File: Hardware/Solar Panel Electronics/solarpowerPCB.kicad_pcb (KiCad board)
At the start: 4 copper layers, 57.8 x 69.2 mm, 151 parts, among them J1 Screw_Terminal_SolarPanel_Inp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, J10 Screw_Terminal_SolarPanel_Inp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, J11 Screw_Terminal_SolarPanel_Inp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, J12 NTC Connector, J13 Battery Connector, J14 Screw_Terminal_5VRail, J2 Screw_Terminal_SolarPanel_Inp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, J3 Conn_01x02_Male, J4 Conn_01x06_Male, J5 Conn_01x02_Male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

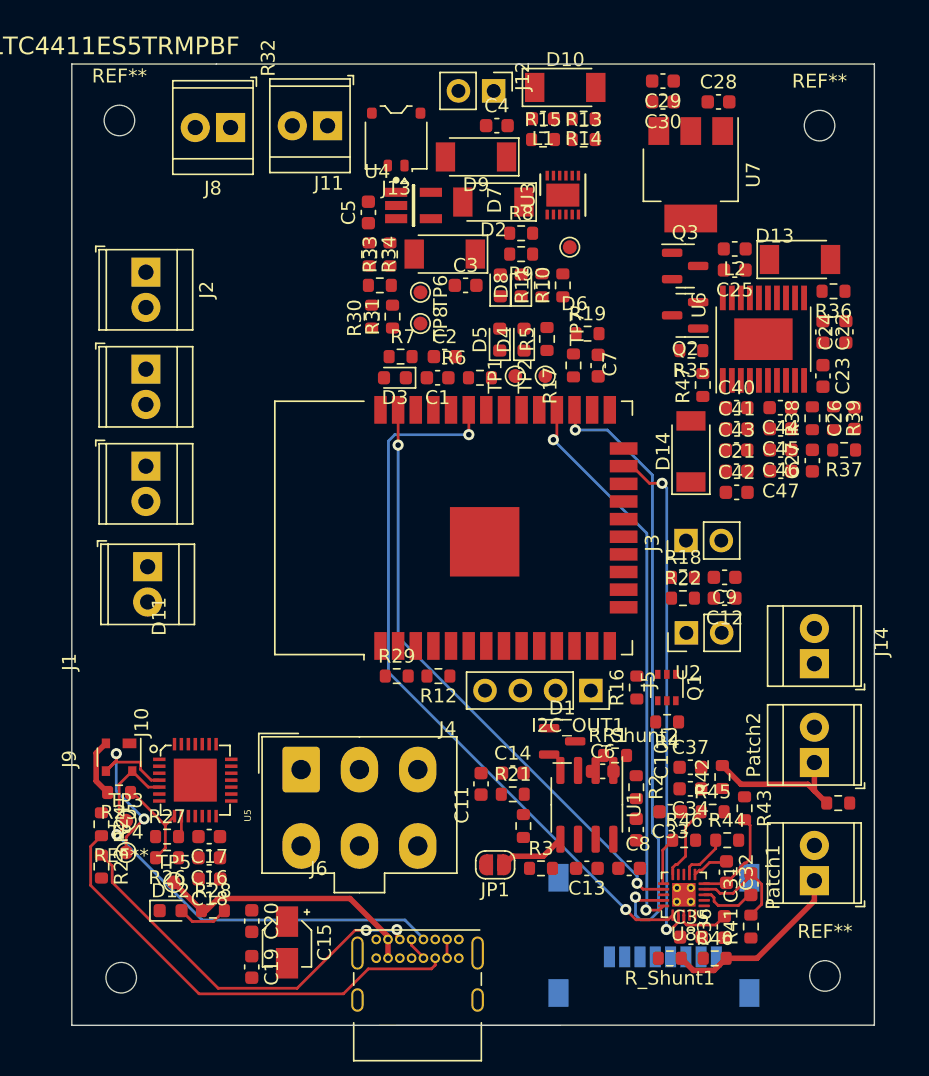
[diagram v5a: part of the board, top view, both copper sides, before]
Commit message: Added another ADS component. Layout and routing can be continued.
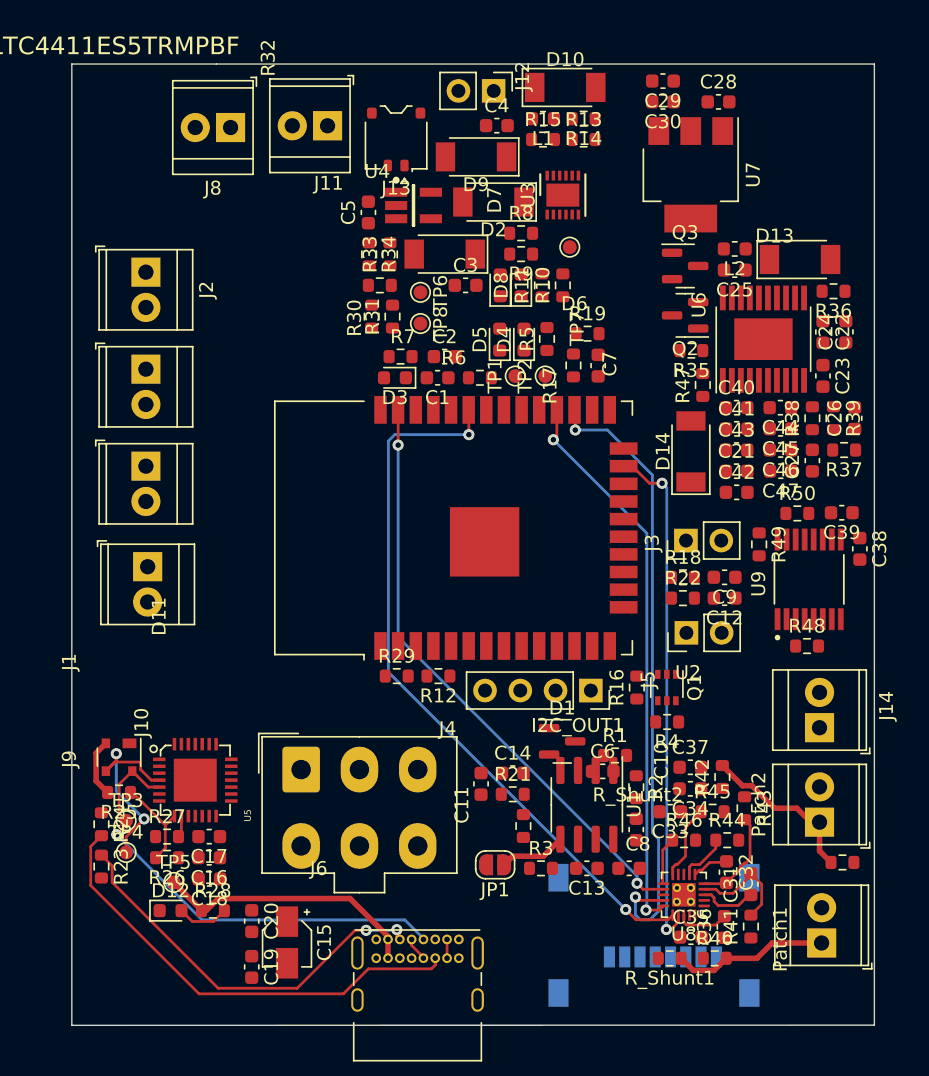
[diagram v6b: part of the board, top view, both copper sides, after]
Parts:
- removed REF** (x4): MountingHole_2.2mm_M2, MountingHole:MountingHole_2.2mm_M2
- added C38: 0.1uF, Capacitor_SMD:C_0603_1608Metric, F.Cu at (82.9, 102.5)
- added C39: 10uF, Capacitor_SMD:C_0603_1608Metric, F.Cu at (81.6, 99.9)
- added R48: 10k, Resistor_SMD:R_0603_1608Metric, F.Cu at (79.1, 109.5)
- added R49: 1k, Resistor_SMD:R_0603_1608Metric, F.Cu at (75.7, 102.2)
- added R50: 1k, Resistor_SMD:R_0603_1608Metric, F.Cu at (78.4, 99.9)
- added U9: ADS1219IPWT, ADS1219IPWT:SOP65P640X120-16N, F.Cu at (79.2, 104.7)
- moved J14 4.62 mm to (80.0, 115.3)
- moved Patch1 4.52 mm to (80.2, 130.8)
- moved Patch2 4.31 mm to (80.0, 122.2)
- moved R_Shunt2 4.28 mm to (81.7, 125.0)
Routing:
- net Net-(Patch1-Pad1): track 13.5 -> 11.3 mm
- net Net-(Patch2-Pad1): track 10.7 -> 11.9 mm

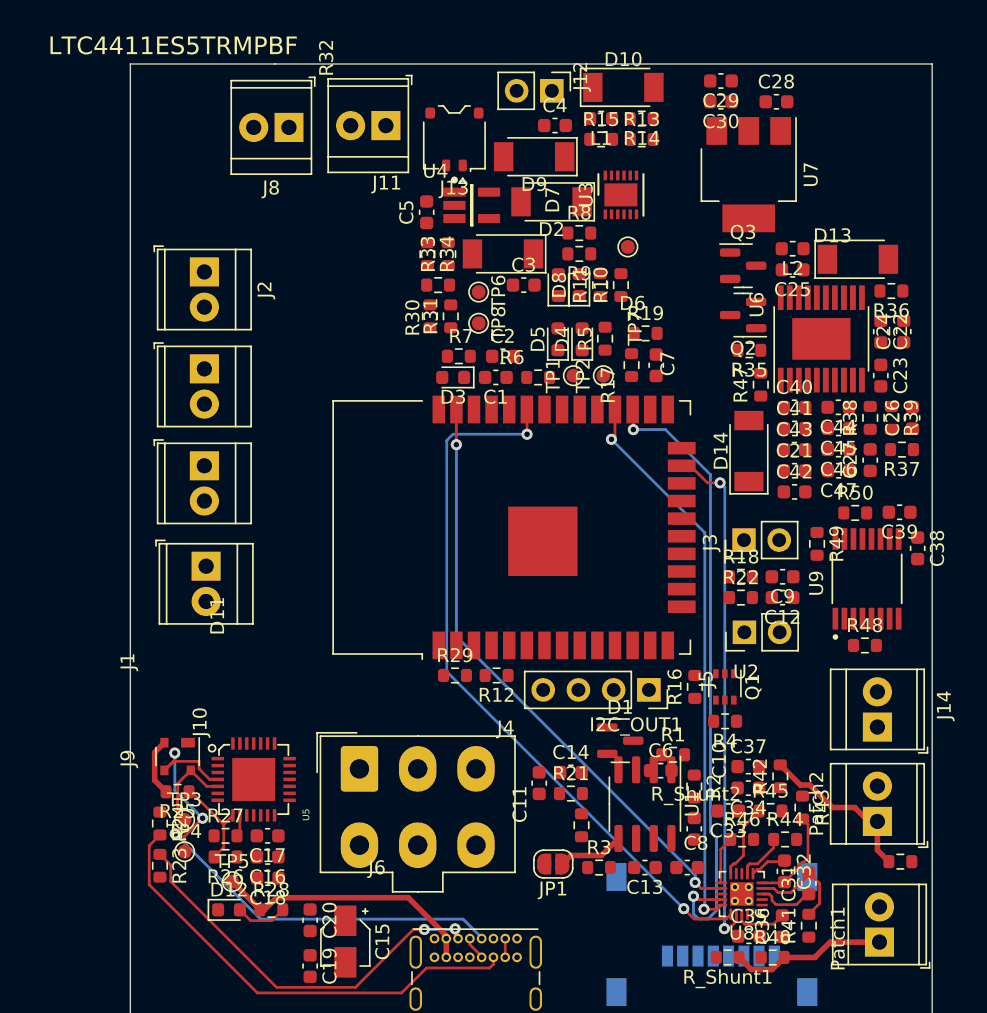
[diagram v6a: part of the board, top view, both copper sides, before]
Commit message: Top half routing done
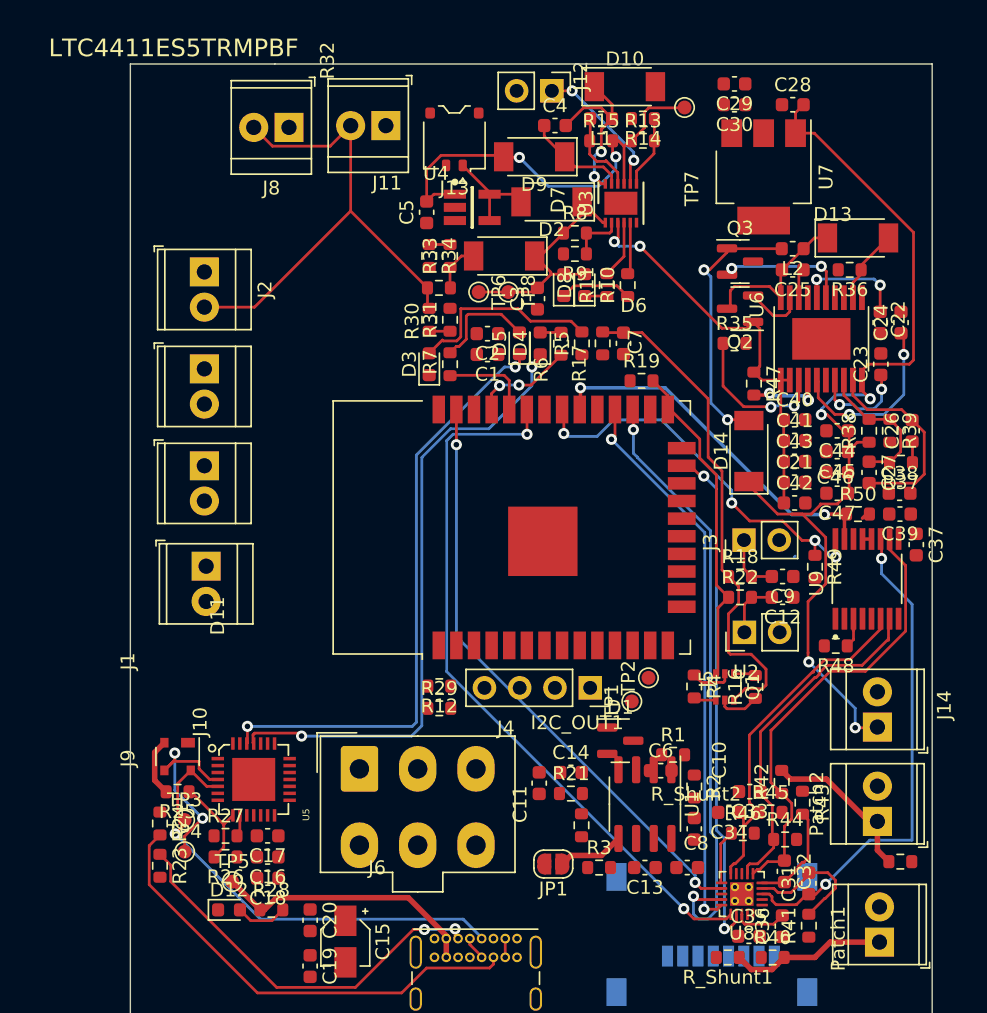
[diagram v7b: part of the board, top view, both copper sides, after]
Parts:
- moved TP1 23.8 mm to (62.3, 113.5)
- moved TP2 22.0 mm to (63.5, 111.8)
- moved C37 20.1 mm to (82.8, 102.2), turned to -90 degrees
- moved TP7 10.8 mm to (66.1, 70.7)
- moved R16 4.36 mm to (71.2, 112.5)
- moved I2C_OUT1 4.24 mm to (59.3, 112.5)
- moved R12 4.20 mm to (48.4, 112.4)
- moved C38 4.18 mm to (81.6, 98.5), turned to 0 degrees
- moved R19 3.43 mm to (63.0, 90.4)
- moved R36 3.37 mm to (78.0, 82.4)
- moved R4 3.35 mm to (66.8, 112.4), turned to -90 degrees
- moved TP8 3.10 mm to (53.4, 84.0)
- moved D4 3.04 mm to (55.7, 87.7)
- moved R6 2.94 mm to (57.2, 87.7), turned to 90 degrees
- moved C7 2.84 mm to (61.7, 87.7)
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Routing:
- net /VoltageReg/V_reg: track 0.00 -> 71.9 mm, vias 0 -> 4
- net /VSolCharger: track 0.00 -> 47.9 mm, vias 0 -> 2
- net /RXD: track 0.00 -> 45.2 mm, vias 0 -> 2
- net /TXD: track 0.00 -> 43.6 mm, vias 0 -> 2
- net /Solar Charger/V_solarpanel: track 0.00 -> 37.1 mm
- net /EN: track 0.00 -> 36.2 mm
- net Net-(C5-Pad2): track 0.00 -> 32.0 mm, vias 0 -> 2
- net /ADC/AIN0P: track 4.15 -> 35.9 mm, vias 0 -> 2
- net /ADC/AIN1P: track 2.66 -> 32.7 mm
- net /SCL: track 0.00 -> 29.0 mm, vias 0 -> 4
- net /SDA: track 0.00 -> 26.4 mm, vias 0 -> 2
- net /BOOT: track 0.00 -> 23.9 mm
- net /ADC/AIN2P: track 3.59 -> 25.4 mm
- net /ADC/AIN3P: track 5.43 -> 25.9 mm
- net Net-(D14-Pad2): track 0.00 -> 19.5 mm, vias 0 -> 2
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
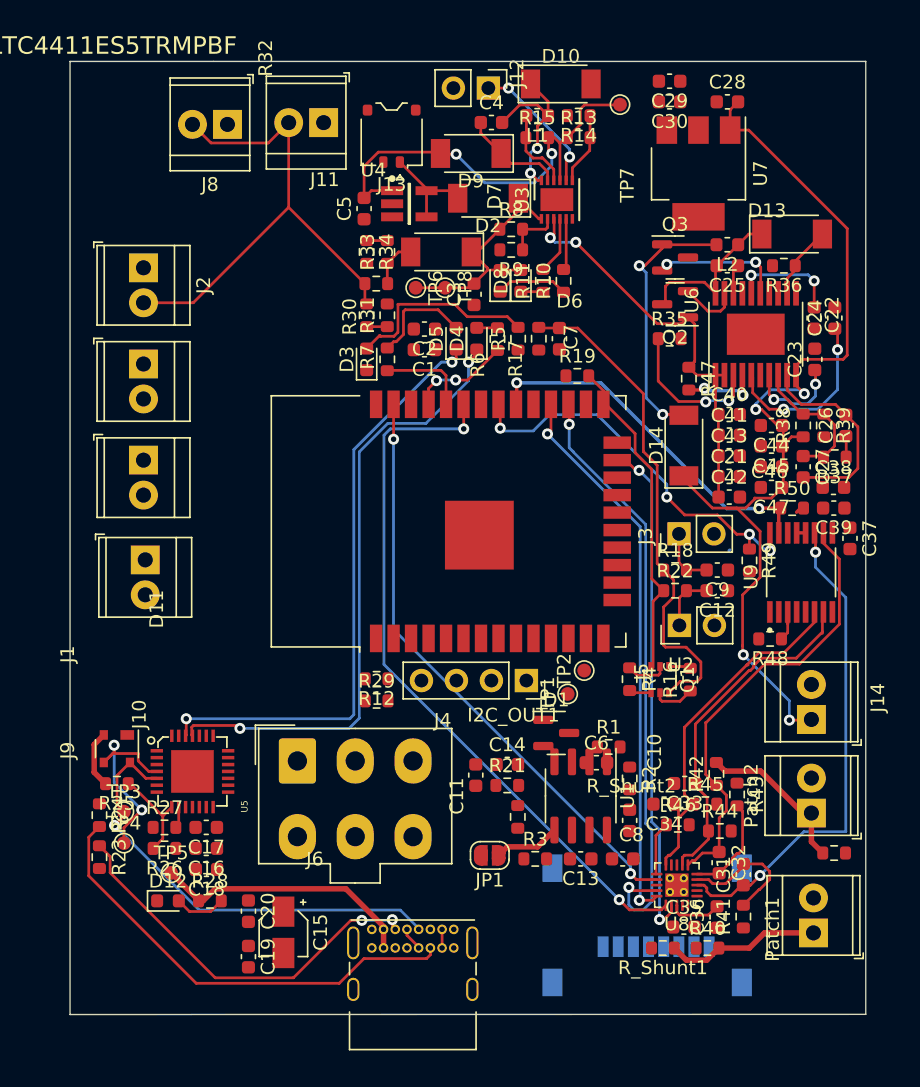
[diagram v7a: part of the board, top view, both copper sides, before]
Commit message: majority of routing done
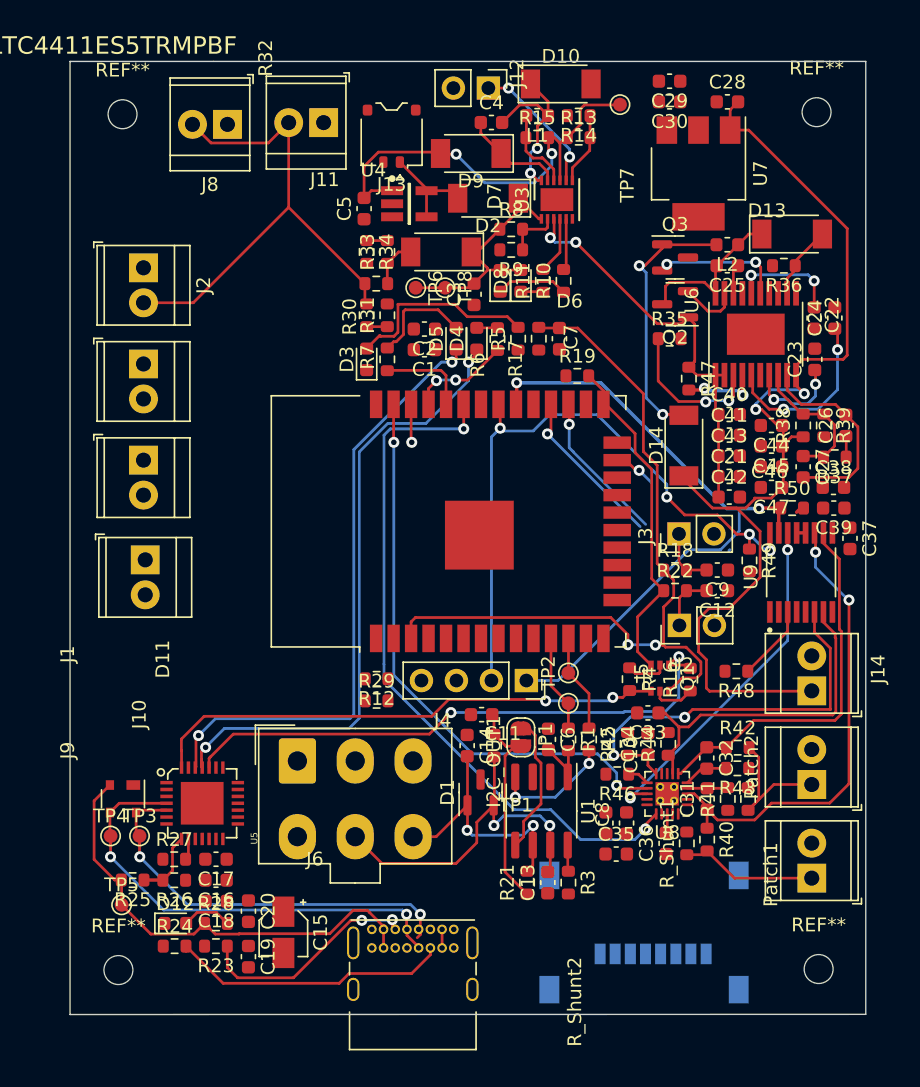
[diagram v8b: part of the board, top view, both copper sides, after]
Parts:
- added REF**: MountingHole_2.1mm, MountingHole:MountingHole_2.1mm, F.Cu at (29.7, 133.6)
- added REF**: MountingHole_2.1mm, MountingHole:MountingHole_2.1mm, F.Cu at (80.5, 133.5)
- added REF**: MountingHole_2.1mm, MountingHole:MountingHole_2.1mm, F.Cu at (80.4, 71.2)
- added REF**: MountingHole_2.1mm, MountingHole:MountingHole_2.1mm, F.Cu at (30.0, 71.4)
- moved R24 11.0 mm to (33.8, 131.8), turned to 0 degrees
- moved R23 10.6 mm to (36.8, 131.8), turned to 180 degrees
- moved JP1 8.86 mm to (58.9, 116.7), turned to -90 degrees
- moved R41 8.62 mm to (73.9, 121.1)
- moved R40 7.88 mm to (72.4, 124.1), turned to -90 degrees
- moved R_Shunt1 7.80 mm to (71.0, 124.3), turned to 90 degrees
- moved C32 7.65 mm to (72.4, 118.2)
- moved R_Shunt2 7.38 mm to (75.4, 121.1), turned to 90 degrees
- moved R44 7.35 mm to (69.6, 117.1), turned to 90 degrees
- moved C35 7.23 mm to (65.8, 125.1)
- moved R21 7.20 mm to (59.4, 127.2), turned to 90 degrees
- moved R45 7.15 mm to (66.7, 117.1), turned to 90 degrees
- moved R25 7.09 mm to (30.7, 127.0)
- moved D1 6.99 mm to (56.0, 120.7), turned to 90 degrees
- moved U8 6.67 mm to (69.5, 120.8)
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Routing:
- net /RTS: track 1.60 -> 42.3 mm, vias 0 -> 2
- net /DTR: track 1.62 -> 37.7 mm, vias 0 -> 2
- net /CLKOUT: track 36.7 -> 3.19 mm, vias 2 -> 1
- net /VSPI_SCLK: track 44.1 -> 11.0 mm, vias 2 -> 1
- net /VSPI_MISO: track 40.3 -> 11.8 mm, vias 2 -> 1
- net /CAN_HIGH: track 0.00 -> 26.6 mm, vias 0 -> 2
- net /ADC/~{DRDY}: track 0.00 -> 25.3 mm, vias 0 -> 2
- net /SDA: track 26.4 -> 48.0 mm
- net /EN: track 36.2 -> 56.9 mm, vias 0 -> 2
- net /CAN_LOW: track 0.00 -> 19.0 mm, vias 0 -> 2
- net /SCL: track 29.0 -> 47.6 mm
- net /usb_to_uart/Data+: track 16.7 -> 34.1 mm
- net Net-(C11-Pad1): track 0.00 -> 15.9 mm
- net Net-(J6-PadB5): track 33.3 -> 20.6 mm
- net Net-(J6-PadA5): track 28.5 -> 16.4 mm
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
